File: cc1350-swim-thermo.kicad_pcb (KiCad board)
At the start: 4 copper layers, 53.1 x 45.2 mm, 127 parts, among them P1 LMT_70_1, P2 LMT_70_2, P3 SMA FEMALE, P4 USB_OTG, P5 CONN_02X05, Q1 2N7002, SW1 SW_Push, U1 2450BM14G0011T, U2 XMSSJE3G0PA-003, U3 CC1350F128RSM, U4 TLV713, U5 TLC5973, U6 MCP16251, U7 LFB18868MBG9E212, Y1 24MHz, Y2 32.768kHz

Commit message: PCB v1.1
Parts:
- removed the REF** at (109.9, 126.1)
- removed the REF** at (123.6, 124.4)
- removed the REF** at (103.8, 131.4)
- added REF**: VIA-0.6mm, cc1350:VIA-0.6mm, F.Cu at (111.9, 126.0)
- added REF**: VIA-0.6mm, cc1350:VIA-0.6mm, F.Cu at (107.0, 125.9)
- added REF**: VIA-0.6mm, cc1350:VIA-0.6mm, F.Cu at (89.8, 112.6)
- added REF**: VIA-0.6mm, cc1350:VIA-0.6mm, F.Cu at (88.8, 115.8)
- P3: footprint cc1350:sma_female_top -> cc1350:SMA_EdgeMount_Horizontal
- R4: value 2.08K -> 1.5K
- moved REF** 30.7 mm to (87.8, 118.5)
- moved REF** 19.0 mm to (116.5, 120.3)
- moved REF** 18.4 mm to (112.0, 120.6)
- moved REF** 16.2 mm to (104.4, 109.7)
- moved REF** 15.0 mm to (122.9, 116.0)
- moved REF** 14.8 mm to (102.0, 119.0)
- moved REF** 13.0 mm to (114.5, 117.7)
- moved REF** 12.1 mm to (112.1, 117.3)
- moved REF** 11.9 mm to (121.6, 123.5)
- moved REF** 11.6 mm to (124.2, 107.2)
- moved REF** 10.0 mm to (122.8, 119.5)
- moved P3 9.80 mm to (109.4, 124.1), turned to 90 degrees
- moved REF** 8.74 mm to (104.2, 115.1)
- moved REF** 8.36 mm to (101.5, 127.8)
- moved REF** 8.12 mm to (121.7, 112.6)
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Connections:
- P4 pad 2: (no net) -> Net-(P4-Pad2)
- P4 pad 3: (no net) -> Net-(P4-Pad3)
- P4 pad 4: (no net) -> Net-(P4-Pad4)
- P5 pad 7: (no net) -> Net-(P5-Pad7)
- U4 pad 4: (no net) -> Net-(U4-Pad4)
- U5 pad 5: (no net) -> Net-(U5-Pad5)
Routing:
- net GND: track 370.1 -> 274.1 mm, vias 58 -> 49
- net /DIO0_RF_SW_PWR: track 19.6 -> 12.7 mm
- net /DIO1_RF_SW: track 18.1 -> 12.0 mm
- net Net-(C8-Pad1): track 20.4 -> 14.9 mm
- net Net-(C13-Pad1): track 4.78 -> 9.96 mm
- net Net-(C5-Pad2): track 9.55 -> 6.08 mm
- net Net-(C4-Pad2): track 9.54 -> 6.08 mm
- net Net-(C20-Pad2): track 6.21 -> 4.07 mm
- net Net-(AE1-Pad1): track 11.7 -> 13.5 mm
- net Net-(C20-Pad1): track 6.98 -> 5.30 mm
- net Net-(U2-Pad10): track 2.88 -> 2.18 mm
- net Net-(U2-Pad1): track 2.86 -> 2.21 mm
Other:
- board size 53.1 x 45.2 mm -> 53.1 x 41.8 mm
- board text added: "Sensor node/concentrator CC1350 sub-GHz and BLE @mik4el4ndersson v1.1"
- board text removed: "Sensor node/concentrator CC1350 sub-GHz and BLE USB or 2xAAA battery @mik4el4ndersson v1 2017"

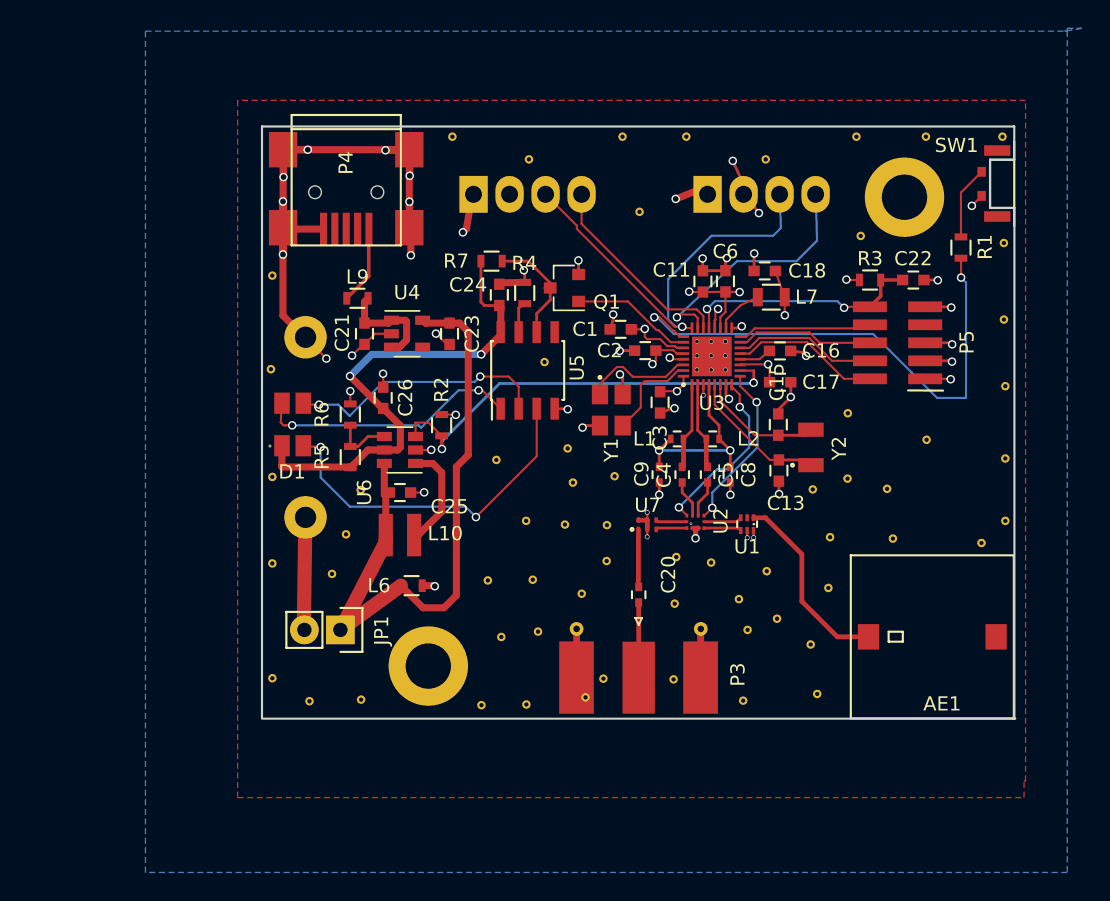
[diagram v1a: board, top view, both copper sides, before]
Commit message: PCB v1.2 ready for manufacturing
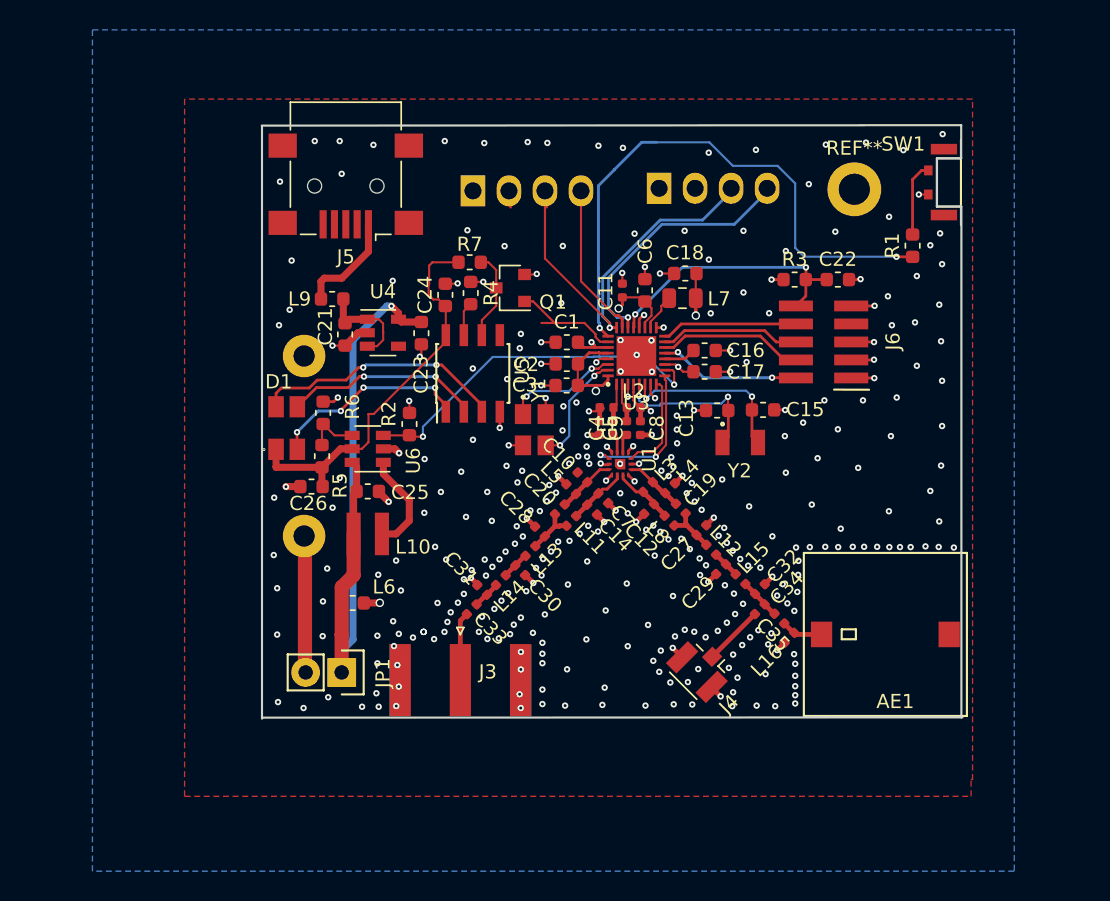
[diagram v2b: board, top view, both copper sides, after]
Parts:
- removed P1: LMT_70_1, Connectors_Molex:Molex_KK-6410-04_04x2.54mm_Straight
- removed P2: LMT_70_2, Connectors_Molex:Molex_KK-6410-04_04x2.54mm_Straight
- removed P3: SMA FEMALE, cc1350:SMA_EdgeMount_Horizontal
- removed P4: USB_OTG, Connectors:USB_Mini-B
- removed P5: CONN_02X05, cc1350:Pin_Header_Straight_SMT_02x05_1_27mm
- removed the REF** at (111.9, 126.0)
- removed the REF** at (113.5, 103.2)
- removed the REF** at (115.5, 102.2)
- removed the REF** at (114.5, 102.2)
- removed the REF** at (112.0, 120.6)
- removed the REF** at (102.8, 103.6)
- removed the REF** at (109.5, 93.0)
- removed the REF** at (107.2, 117.6)
- removed the REF** at (101.5, 114.8)
- removed the REF** at (107.2, 115.1)
- removed the REF** at (104.2, 115.1)
- removed the REF** at (107.0, 125.9)
- removed the REF** at (124.2, 107.2)
- removed the REF** at (124.2, 111.8)
- removed the REF** at (121.6, 123.5)
- removed the REF** at (129.8, 109.1)
- removed the REF** at (114.5, 117.7)
- removed the REF** at (116.5, 120.3)
- removed the REF** at (127.0, 112.5)
- removed the REF** at (125.1, 94.7)
- removed the REF** at (135.2, 95.2)
- removed the REF** at (135.2, 100.6)
- removed the REF** at (89.8, 112.6)
- removed the REF** at (135.3, 105.3)
- removed the REF** at (135.3, 110.4)
- removed the REF** at (135.3, 114.8)
- removed the REF** at (133.6, 116.4)
- removed the REF** at (127.4, 116.0)
- removed the REF** at (121.7, 112.6)
- removed the REF** at (116.8, 127.5)
- removed the REF** at (122.9, 116.0)
- removed the REF** at (105.4, 119.9)
- removed the REF** at (102.3, 122.6)
- removed the REF** at (88.8, 115.8)
- removed the REF** at (105.7, 127.2)
- removed the REF** at (104.4, 109.7)
- removed the REF** at (119.2, 121.7)
- removed the REF** at (87.8, 118.5)
- removed the REF** at (122.0, 127.0)
- removed the REF** at (118.5, 118.3)
- removed the REF** at (112.1, 117.3)
- removed the REF** at (122.8, 119.5)
- removed the REF** at (117.1, 122.5)
- removed the REF** at (102.0, 119.0)
- removed the REF** at (115.5, 104.2)
- removed the REF** at (99.4, 110.5)
- removed the REF** at (104.8, 112.1)
- removed the REF** at (107.7, 111.7)
- removed the REF** at (98.8, 119.0)
- removed the REF** at (99.8, 123.0)
- removed the REF** at (101.5, 127.8)
- removed the REF** at (98.3, 127.8)
- removed the REF** at (89.9, 127.4)
- removed the REF** at (86.2, 127.5)
- removed the REF** at (83.6, 125.9)
- removed the REF** at (114.5, 104.2)
- removed the REF** at (83.6, 117.8)
- removed the REF** at (83.6, 111.7)
- removed the REF** at (83.5, 104.1)
- removed the REF** at (83.6, 97.5)
- removed the REF** at (96.3, 87.7)
- removed the REF** at (101.7, 89.3)
- removed the REF** at (108.3, 87.7)
- removed the REF** at (112.8, 87.7)
- removed the REF** at (118.4, 89.3)
- removed the REF** at (124.8, 87.7)
- removed the REF** at (113.5, 104.2)
- removed the REF** at (129.7, 87.7)
- removed the REF** at (94.6, 125.0)
- removed the REF** at (128.2, 92.0)
- removed the REF** at (135.1, 87.7)
- removed the REF** at (113.5, 102.2)
- removed the REF** at (115.5, 103.2)
- removed the REF** at (114.5, 103.2)
- removed U2: XMSSJE3G0PA-003, cc1350:XMSSJE3G0PA-003
- removed U7: LFB18868MBG9E212, cc1350:LFB18868MBG9E212
- added C10: 3.6pF, Capacitor_SMD:C_0402_1005Metric, F.Cu at (105.5, 111.7)
- added C12: 1pF, Capacitor_SMD:C_0402_1005Metric, F.Cu at (110.2, 114.0)
- added C14: 3.6pF, Capacitor_SMD:C_0402_1005Metric, F.Cu at (106.2, 114.0)
- added C19: 1pF, Capacitor_SMD:C_0402_1005Metric, F.Cu at (112.4, 113.9)
- added C27: DNM, Capacitor_SMD:C_0402_1005Metric, F.Cu at (113.9, 115.5)
- added C28: 3.6pF, Capacitor_SMD:C_0402_1005Metric, F.Cu at (102.5, 115.5)
- added C29: 3.6pF, Capacitor_SMD:C_0402_1005Metric, F.Cu at (115.2, 118.2)
- added C30: 5.6pF, Capacitor_SMD:C_0402_1005Metric, F.Cu at (101.1, 118.3)
- added C31: 3.3pF, Capacitor_SMD:C_0402_1005Metric, F.Cu at (98.4, 119.7)
- added C32: 1pF, Capacitor_SMD:C_0402_1005Metric, F.Cu at (118.0, 119.6)
- added C33: 100pF, Capacitor_SMD:C_0402_1005Metric, F.Cu at (97.7, 121.0)
- added C34: DNM, Capacitor_SMD:C_0402_1005Metric, F.Cu at (118.0, 121.0)
- added C35: 100pF, Capacitor_SMD:C_0402_1005Metric, F.Cu at (119.4, 121.7)
- added C7: 3.6pF, Capacitor_SMD:C_0402_1005Metric, F.Cu at (106.9, 113.2)
- added J1: LMT_70_1, Connector_Molex:Molex_KK-254_AE-6410-04A_1x04_P2.54mm_Vertical, B.Cu at (110.9, 91.3)
- added J2: LMT_70_2, Connector_Molex:Molex_KK-254_AE-6410-04A_1x04_P2.54mm_Vertical, B.Cu at (97.8, 91.5)
- added J3: SMA, Connector_Coaxial:SMA_Amphenol_132289_EdgeMount, F.Cu at (96.9, 126.0)
- added J4: U.FL, cc1350:U.FL_Hirose_U.FL-R-SMT-1_Vertical, F.Cu at (113.9, 125.1)
- added J5: USB_B_Micro, Connector_USB:USB_Mini-B_Lumberg_2486_01_Horizontal, F.Cu at (88.8, 91.2)
- added J6: Conn_02x05_Odd_Even, cc1350:Pin_Header_Straight_SMT_02x05_1_27mm, F.Cu at (122.4, 102.1)
- added L11: 6.8nH, Inductor_SMD:L_0402_1005Metric, F.Cu at (104.7, 114.8)
- added L12: 1.5nH, Inductor_SMD:L_0402_1005Metric, F.Cu at (114.6, 116.8)
- added L13: 6.8nH, Inductor_SMD:L_0402_1005Metric, F.Cu at (101.8, 116.9)
- added L14: 7.5nH, Inductor_SMD:L_0402_1005Metric, F.Cu at (99.7, 119.0)
- added L15: 2.2nH, Inductor_SMD:L_0402_1005Metric, F.Cu at (116.6, 118.9)
- added L16: DNM, Inductor_SMD:L_0402_1005Metric, F.Cu at (120.1, 123.0)
- added L3: DNM, Inductor_SMD:L_0402_1005Metric, F.Cu at (110.1, 112.4)
- added L4: 2.2nH, Inductor_SMD:L_0402_1005Metric, F.Cu at (111.6, 112.5)
- added L5: 6.8nH, Inductor_SMD:L_0402_1005Metric, F.Cu at (104.7, 112.6)
- added L8: 2.2nH, Inductor_SMD:L_0402_1005Metric, F.Cu at (111.6, 114.8)
- added REF**: MountingHole_2.2mm_M2_DIN965_Pad, MountingHole:MountingHole_2.2mm_M2_DIN965_Pad, F.Cu at (124.7, 91.4)
- C1, C13, C15, C16, C17, C18, C2, C21, C22, C23, C24, C25, C26, C3, C6: footprint Capacitors_SMD:C_0603 -> Capacitor_SMD:C_0603_1608Metric
- C11: footprint Capacitors_SMD:C_0603 -> Capacitor_SMD:C_0402_1005Metric
- C20: value 100pF -> 3.6pF; footprint Capacitors_SMD:C_0402 -> Capacitor_SMD:C_0402_1005Metric
- C4, C5, C8, C9: footprint Capacitors_SMD:C_0402 -> Capacitor_SMD:C_0402_1005Metric
- L1, L2: footprint Resistors_SMD:R_0402 -> Inductor_SMD:L_0402_1005Metric
- L6, L9: footprint Resistors_SMD:R_0603 -> Inductor_SMD:L_0603_1608Metric
- L7: footprint Resistors_SMD:R_0805 -> Inductor_SMD:L_0805_2012Metric
- R1, R2, R3, R4, R5, R6, R7: footprint Resistors_SMD:R_0603 -> Resistor_SMD:R_0603_1608Metric
- U1: value 2450BM14G0011T -> SKY13421-486LF; footprint cc1350:2450BM14G011T -> cc1350:SKY13421-486LF
- moved U1 10.1 mm to (107.6, 111.4), turned to 90 degrees
- moved C20 8.20 mm to (103.9, 114.0), turned to 45 degrees
- moved C26 8.05 mm to (86.4, 112.4), turned to 180 degrees
- moved C8 7.14 mm to (109.6, 108.3)
- moved C3 6.70 mm to (104.4, 105.2), turned to 180 degrees
- moved C5 6.59 mm to (108.6, 108.3)
- moved L7 6.26 mm to (112.5, 99.1)
- moved C13 6.08 mm to (115.0, 107.0), turned to 180 degrees
- moved L2 6.00 mm to (109.1, 106.8)
- moved C4 5.88 mm to (107.6, 108.3)
- moved C6 5.72 mm to (109.9, 98.5)
- moved C11 5.72 mm to (108.3, 98.5)
- moved C2 5.61 mm to (104.4, 103.7)
- moved C18 5.61 mm to (112.7, 97.3)
- moved Y1 5.61 mm to (102.1, 108.4)
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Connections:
- C20 pad 2: Net-(C20-Pad2) -> /868_RF_P
- C4 pad 1: Net-(C4-Pad1) -> /BIAS_RF_P
- C5 pad 1: Net-(C5-Pad1) -> /BIAS_RF_N
- U1 pad 1: Net-(AE1-Pad1) -> GND
- U1 pad 3: Net-(U1-Pad3) -> /2_4_RF_P
- U1 pad 4: Net-(U1-Pad4) -> GND
- U1 pad 5: GND -> /2_4_RF_N
- U3 pad : (no net) -> GND
- U4 pad 4: Net-(U4-Pad4) -> (no net)
- U5 pad 1: Net-(D1-Pad2) -> Net-(D1-Pad4)
- U5 pad 3: Net-(D1-Pad4) -> Net-(D1-Pad2)
- U5 pad 5: Net-(U5-Pad5) -> (no net)
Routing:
- net GND: track 274.1 -> 54.9 mm, vias 49 -> 338
- net /VDDS: track 111.5 -> 13.4 mm, vias 9 -> 6
- net Net-(D1-Pad4): track 25.5 -> 14.3 mm, vias 2 -> 4
- net Net-(AE1-Pad1): track 13.5 -> 2.95 mm
- net +5V: track 35.2 -> 27.7 mm, vias 2 -> 0
- net /T_ON_2: track 18.2 -> 11.0 mm, vias 1 -> 0
- net /DIO0_RF_SW_PWR: track 12.7 -> 7.07 mm, vias 2 -> 0
- net Net-(C8-Pad1): track 14.9 -> 9.87 mm
- net Net-(D1-Pad3): track 18.9 -> 13.9 mm
- net Net-(C33-Pad1): track 0.00 -> 4.84 mm
- net /PSU_ENABLE: track 30.3 -> 25.8 mm
- net /2_4_RF_P: track 0.00 -> 4.38 mm
- net /868_RF_N: track 0.00 -> 4.29 mm
- net Net-(C34-Pad1): track 0.00 -> 4.26 mm
- net /868_RF_P: track 0.00 -> 4.14 mm
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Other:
- board size 53.1 x 41.8 mm -> 49.4 x 41.9 mm
- net class 50ohm: clearance 0.34 -> 0.36
- net class Default: clearance 0.127 -> 0.1
- rule trace_clearance: 0.127 -> 0.1
- rule trace_min: 0.127 -> 0.089
- rule via_min_drill: 0.254 -> 0.2
- rule via_min_size: 0.3 -> 0.45
- board text added: "Sensor node/concentrator CC1350 sub-GHz and BLE @mik4el4ndersson v1.2"
- board text removed: "Sensor node/concentrator CC1350 sub-GHz and BLE @mik4el4ndersson v1.1"

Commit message: PCB sent to manufacturing
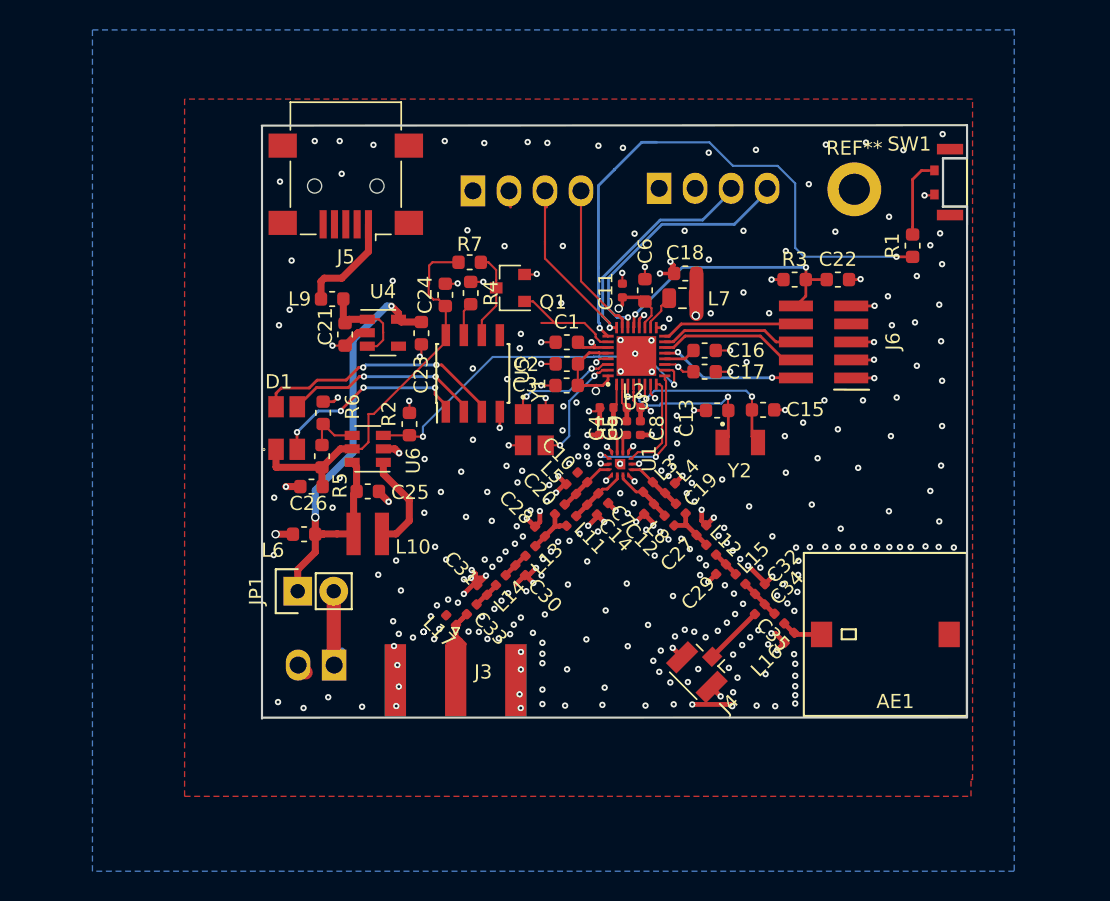
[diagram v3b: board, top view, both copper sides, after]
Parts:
- added L17: DNM, Inductor_SMD:L_0402_1005Metric, F.Cu at (96.2, 121.8)
- BT1: footprint cc1350:2_AAA_batteryholder_keystone -> Connector_Molex:Molex_KK-254_AE-6410-02A_1x02_P2.54mm_Vertical
- moved BT1 9.34 mm to (88.0, 125.0)
- moved JP1 6.51 mm to (85.4, 119.8), turned to 90 degrees
- moved L6 5.94 mm to (85.8, 115.7), turned to 0 degrees
- moved SW1 0.43 mm to (132.6, 90.9)
- moved J3 0.33 mm to (96.5, 126.0)
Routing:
- net GND: track 54.9 -> 74.2 mm, vias 338 -> 332
- net VCC: track 45.7 -> 33.8 mm, vias 1 -> 2
- net Net-(C33-Pad1): track 4.84 -> 10.1 mm
- net Net-(BT1-Pad1): track 9.81 -> 6.74 mm
- net /VDDR: track 19.2 -> 22.1 mm
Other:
- board size 49.4 x 41.9 mm -> 49.8 x 41.9 mm

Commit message: pcb revision v1.3 after tests
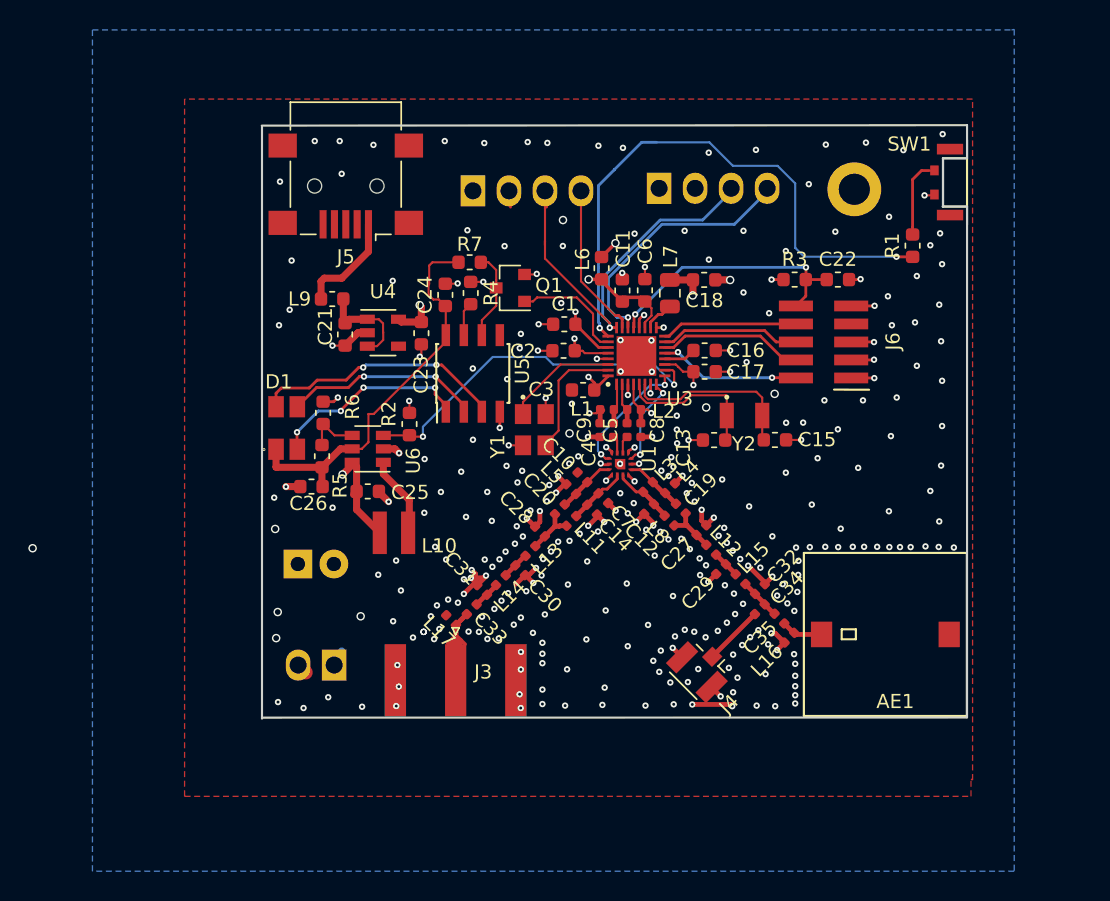
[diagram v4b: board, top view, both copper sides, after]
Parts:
- C11: footprint Capacitor_SMD:C_0402_1005Metric -> Capacitor_SMD:C_0603_1608Metric
- JP1: moved to B.Cu
- moved L6 28.1 mm to (106.8, 97.0), turned to 90 degrees
- moved C15 2.28 mm to (119.0, 109.1)
- moved C13 2.10 mm to (114.8, 109.1)
- moved Y2 1.92 mm to (116.9, 107.4)
- moved JP1 1.92 mm to (85.4, 117.8), turned to 270 degrees
- moved L10 1.85 mm to (92.2, 115.6)
- moved C18 1.40 mm to (114.1, 97.8), turned to 0 degrees
- moved C1 1.28 mm to (104.2, 100.9)
- moved C3 1.21 mm to (105.5, 105.6)
- moved C2 0.96 mm to (104.1, 102.8)
- moved L7 0.95 mm to (111.6, 98.7), turned to 270 degrees
- moved C4 0.14 mm to (107.7, 108.4)
- moved C5 0.14 mm to (108.6, 108.4)
- moved C8 0.14 mm to (109.6, 108.4)
- moved C9 0.14 mm to (106.7, 108.4)
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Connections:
- J1 pad 1: /VDDS -> VCC
- J2 pad 1: /VDDS -> VCC
- J6 pad 1: /VDDS -> VCC
- R3 pad 1: /VDDS -> VCC
- U3 pad : GND -> (no net)
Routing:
- net VCC: track 33.8 -> 119.0 mm, vias 2 -> 5
- net /VDDS: track 13.5 -> 28.4 mm, vias 6 -> 3
- net /VDDR: track 22.1 -> 32.3 mm, vias 2 -> 3
- net GND: track 74.2 -> 71.4 mm, vias 332 -> 321
- net Net-(L10-Pad1): track 7.23 -> 4.92 mm
- net Net-(BT1-Pad1): track 6.74 -> 8.70 mm
- net /DIO1_RF_SW: track 10.7 -> 8.83 mm
- net Net-(C13-Pad1): track 11.3 -> 10.5 mm, vias 2 -> 0
- net Net-(U3-Pad31): track 8.04 -> 8.74 mm, vias 2 -> 0
- net /DIO0_RF_SW_PWR: track 7.07 -> 6.57 mm, vias 0 -> 2
- net Net-(C15-Pad1): track 12.3 -> 12.6 mm, vias 2 -> 0
- net Net-(U3-Pad30): track 8.03 -> 7.95 mm, vias 2 -> 0
- net (no net): vias 0 -> 5
- removed copper zone on In2.Cu, net /VDDS
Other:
- board text added: "Sensor node/concentrator CC1350 sub-GHz and BLE @mik4el4ndersson v1.3"
- board text removed: "Sensor node/concentrator CC1350 sub-GHz and BLE @mik4el4ndersson v1.2"
